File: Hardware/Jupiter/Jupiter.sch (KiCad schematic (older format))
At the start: 0 parts

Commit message: Start schematic diagram by placing the first IC components.
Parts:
- added MD?: Board_RPi_CM3lite_200pConnector, _, symbol Board_RPi_CM3lite_200pConnector
- added U?: STM32F070CBT6, symbol STM32F070CBT6
- added U?: ENC28J60, symbol ENC28J60
- added U?: CY7C65632, symbol CY7C65632
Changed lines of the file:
@@
 LIBS:contrib
 LIBS:valves
+LIBS:stm32f070cbt6
+LIBS:MIC2026
+LIBS:KiCADinfo_RPi-modules
+LIBS:enc28j60
+LIBS:cy7c65632
+LIBS:503182-1852
+LIBS:Jupiter-cache
 EELAYER 25 0
 EELAYER END
-$Descr USLetter 11000 8500
+$Descr A2 23386 16535
 encoding utf-8
 Sheet 1 1
@@
 Comment4 ""
 $EndDescr
+$Comp
+L Board_RPi_CM3lite_200pConnector MD?
+U 1 1 5B60D14B
+P 3550 8200
+F 0 "MD?" H 4275 575 50  0000 C CNN
+F 1 "Board_RPi_CM3lite_200pConnector" H 3550 15825 50  0000 C CNN
+F 2 "_" H 3550 8200 10  0001 C CNN
+F 3 "_" H 3550 8200 10  0001 C CNN
+F 4 "_" H 3550 8200 10  0001 C CNN "Manf#"
+F 5 "_" H 3550 8200 10  0001 C CNN "Manf"
+F 6 "_" H 3550 8200 10  0001 C CNN "Optn"
+	1    3550 8200
+	1    0    0    -1
+$EndComp
+$Comp
+L STM32F070CBT6 U?
+U 1 1 5B60D344
+P 9350 3400
+F 0 "U?" H 9350 2650 60  0000 C CNN
+F 1 "STM32F070CBT6" H 9350 2950 60  0000 C CNN
+F 2 "" H 9350 3400 60  0001 C CNN
+F 3 "" H 9350 3400 60  0001 C CNN
+	1    9350 3400
+	1    0    0    -1
+$EndComp
+$Comp
+L ENC28J60 U?
+U 1 1 5B60D397
+P 9100 7900
+F 0 "U?" H 9100 6100 60  0000 C CNN
+F 1 "ENC28J60" H 9100 8400 60  0000 C CNN
+F 2 "" H 9100 7500 60  0000 C CNN
+F 3 "" H 9100 7500 60  0000 C CNN
+	1    9100 7900
+	1    0    0    -1
+$EndComp
+$Comp
+L CY7C65632 U?
+U 1 1 5B60D432
+P 14500 3900
+F 0 "U?" H 14500 3750 60  0000 C CNN
+F 1 "CY7C65632" H 14500 3900 60  0000 C CNN
+F 2 "" H 14500 3900 60  0000 C CNN
+F 3 "" H 14500 3900 60  0000 C CNN
+	1    14500 3900
+	1    0    0    -1
+$EndComp
 $EndSCHEMATC

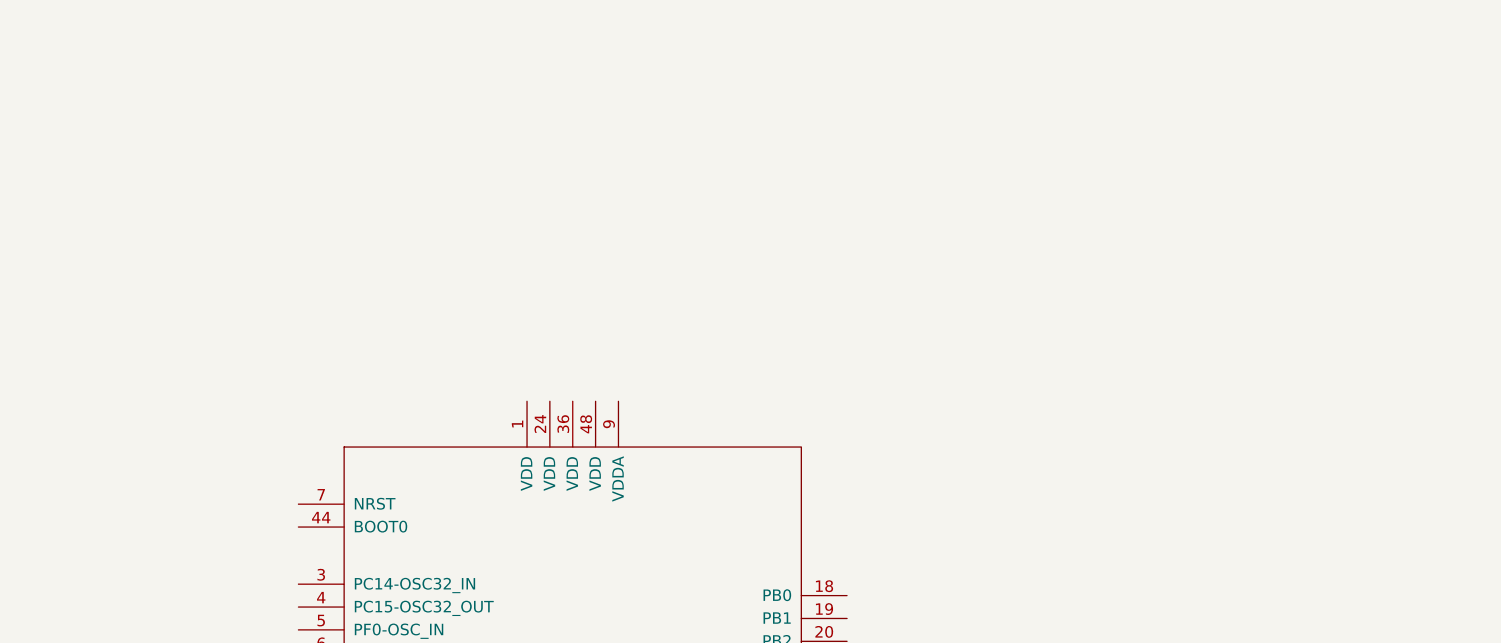
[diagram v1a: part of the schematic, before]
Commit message: Add a power regulator for providing both 3.3v and 1.8v to board.
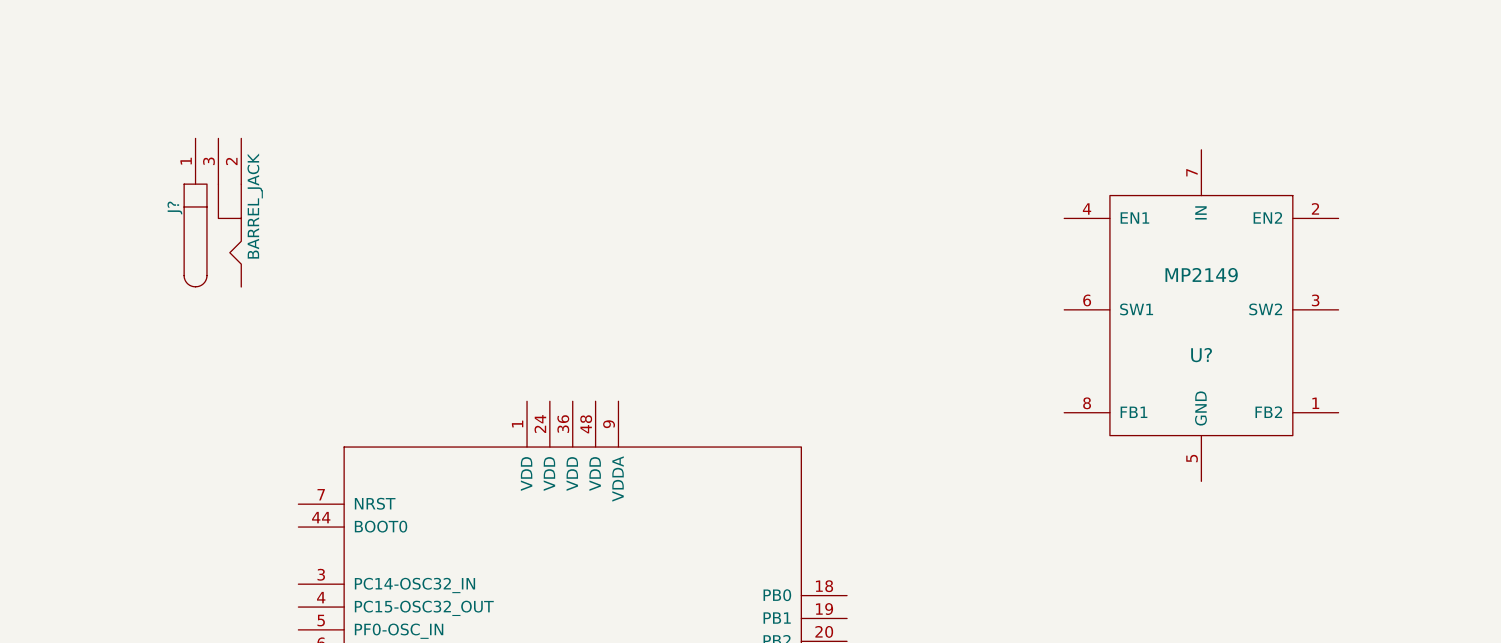
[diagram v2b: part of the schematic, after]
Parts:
- added J?: BARREL_JACK, symbol BARREL_JACK
- added U?: MP2149, symbol MP2149
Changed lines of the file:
@@
 LIBS:cy7c65632
 LIBS:503182-1852
+LIBS:MP2149
 LIBS:Jupiter-cache
 EELAYER 25 0
@@
 	1    0    0    -1
 $EndComp
+$Comp
+L BARREL_JACK J?
+U 1 1 5B60D3BC
+P 7800 1350
+F 0 "J?" H 7800 1545 50  0000 C CNN
+F 1 "BARREL_JACK" H 7800 1195 50  0000 C CNN
+F 2 "" H 7800 1350 50  0001 C CNN
+F 3 "" H 7800 1350 50  0001 C CNN
+	1    7800 1350
+	0    -1   -1   0
+$EndComp
+$Comp
+L MP2149 U?
+U 1 1 5B60D5AD
+P 12100 1800
+F 0 "U?" H 12100 1600 60  0000 C CNN
+F 1 "MP2149" H 12100 1950 60  0000 C CNN
+F 2 "" H 12100 1800 60  0000 C CNN
+F 3 "" H 12100 1800 60  0000 C CNN
+	1    12100 1800
+	1    0    0    -1
+$EndComp

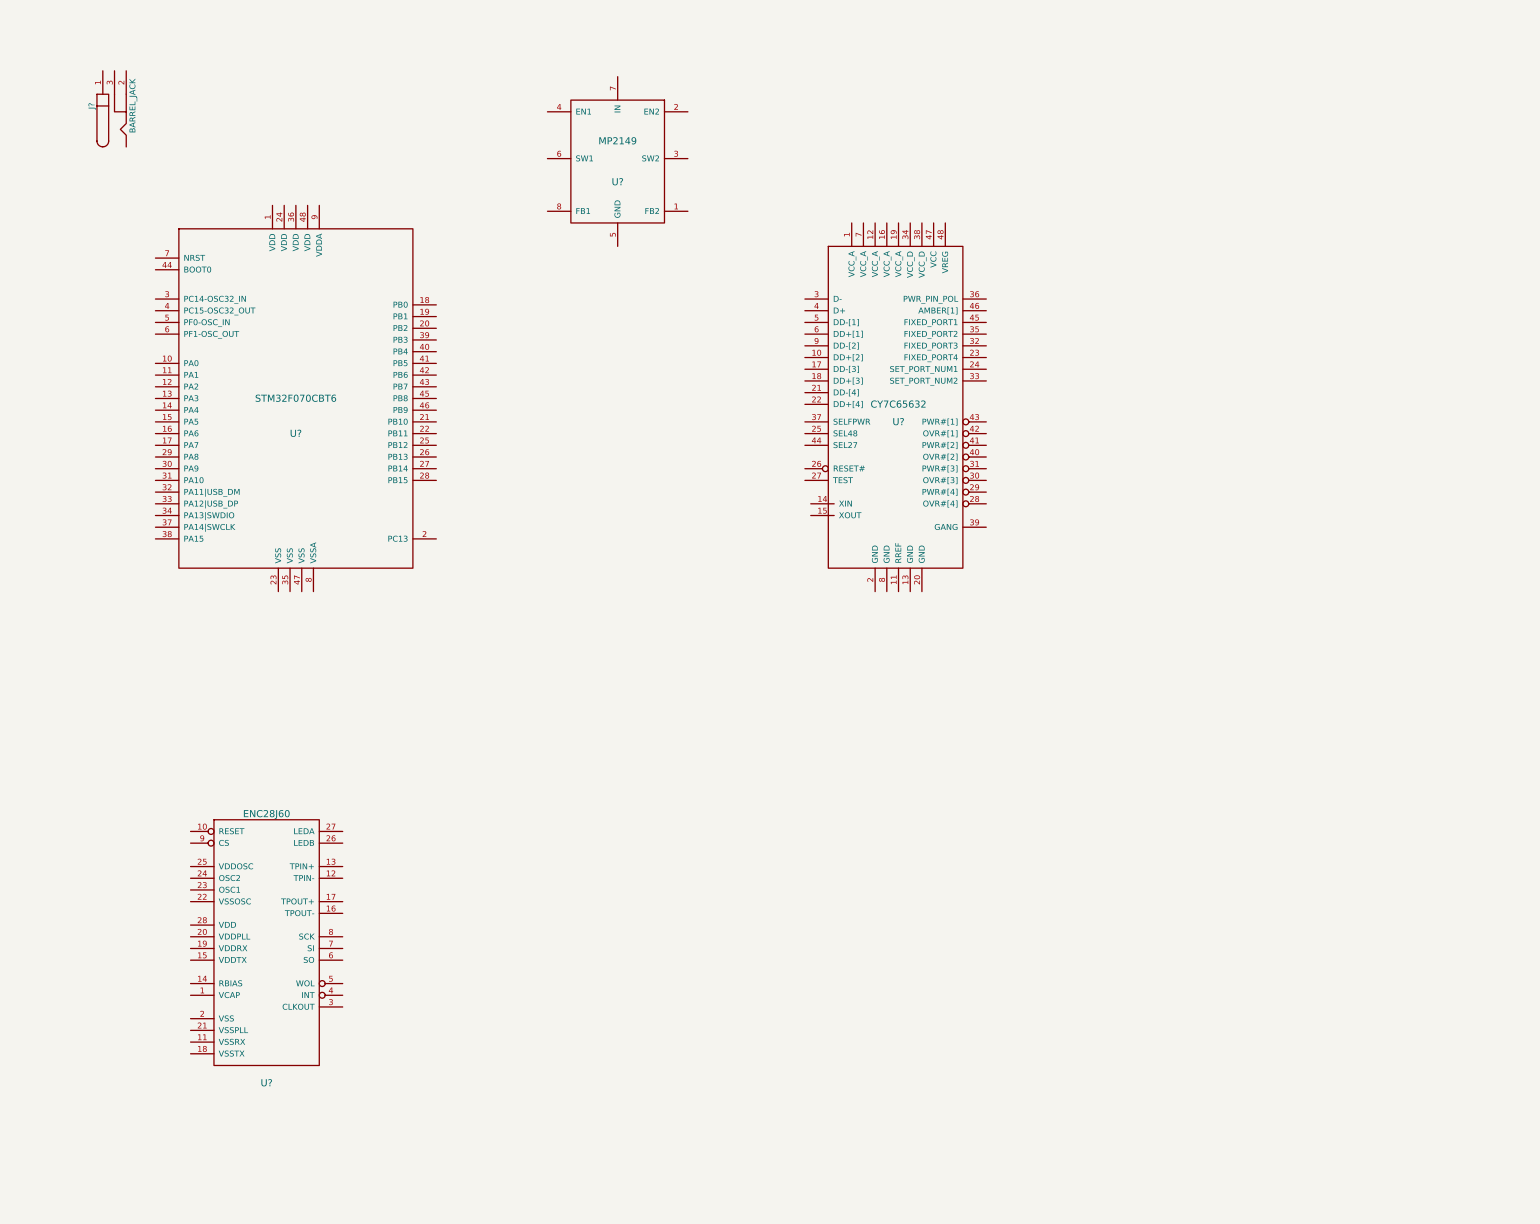
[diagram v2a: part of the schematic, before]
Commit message: Add power input and start work on network adapter chip.
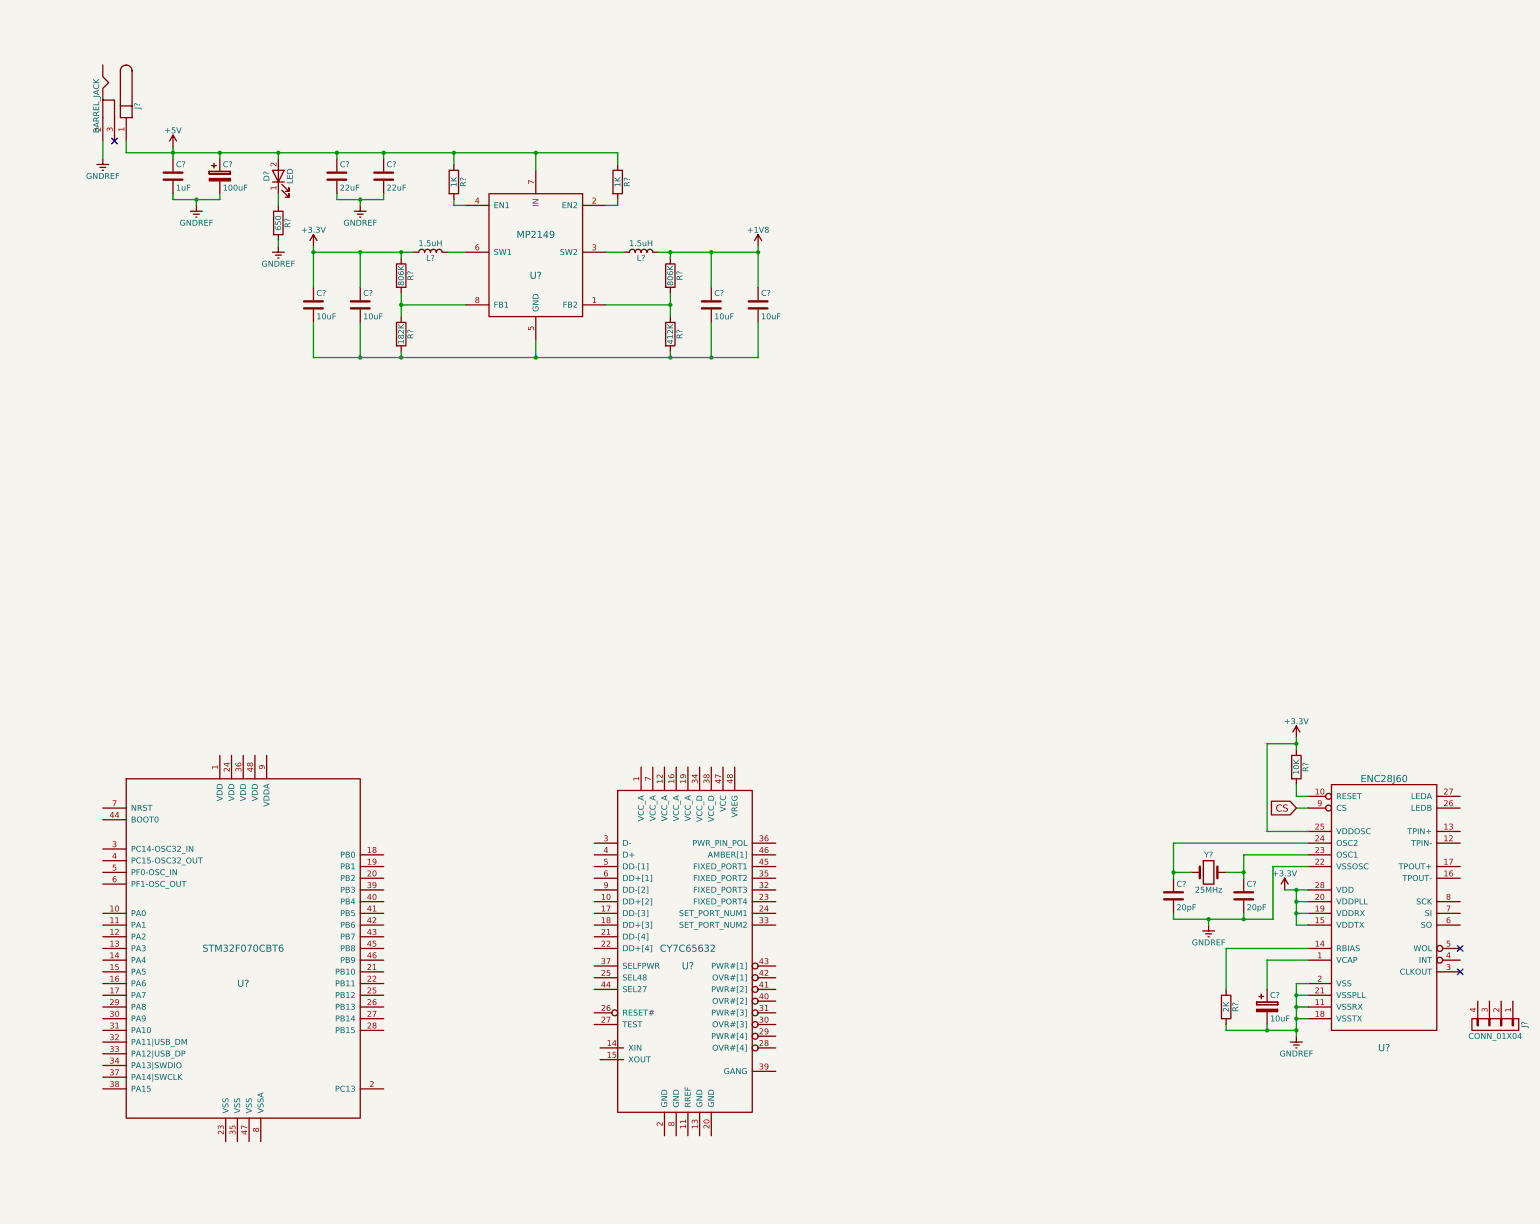
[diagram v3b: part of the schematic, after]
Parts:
- added C?: 1uF, symbol C
- added C?: 100uF, symbol CP
- added C? (x2): 22uF, symbol C
- added C? (x4): 10uF, symbol C
- added C?: 10uF, symbol CP
- added C? (x2): 20pF, symbol C
- added D?: LED, symbol LED
- added J?: CONN_01X04, symbol CONN_01X04
- added L? (x2): 1.5uH, symbol L
- added R?: 650, symbol R
- added R? (x2): 806K, symbol R
- added R?: 182K, symbol R
- added R?: 412K, symbol R
- added R? (x2): 1K, symbol R
- added R?: 10K, symbol R
- added R?: 2K, symbol R
- added Y?: 25MHz, symbol Crystal
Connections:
- net at U?.1 (VCAP): now also C?.1
- net at U?.10 (RESET): now also R?.2
- net GNDREF: now reaches U?.11 (VSSRX)
- net GNDREF: now also J?.2, U?.18 (VSSTX), U?.2 (VSS), U?.21 (VSSPLL), U?.22 (VSSOSC), C?.2, C?.2, C?.2, C?.2, C?.2, C?.2, C?.2, R?.2, R?.2
- net at U?.14 (RBIAS): now also R?.1
- net +3V3: now reaches U?.15 (VDDTX)
- net +3V3: now also U?.19 (VDDRX), U?.20 (VDDPLL), U?.25 (VDDOSC), U?.28 (VDD), C?.1, C?.1, L?.1, R?.1, R?.1
- net at U?.23 (OSC1): now also C?.1, Y?.2
- net at U?.24 (OSC2): now also C?.1, Y?.1
- net CS: now reaches U?.9 (CS)
- net +5V: now reaches J?.1
- net +5V: now also U?.7 (IN), C?.1, C?.1, C?.1, C?.1, D?.2 (A), R?.1, R?.1
- net at U?.1 (FB2): now also R?.1, R?.2
- net at U?.2 (EN2): now also R?.2
- net at U?.3 (SW2): now also L?.1
- net at U?.4 (EN1): now also R?.2
- net at U?.5 (GND): now also C?.2, C?.2, C?.2, C?.2, R?.2, R?.2
- net at U?.6 (SW1): now also L?.2
- net at U?.8 (FB1): now also R?.1, R?.2
- new net: D?.1 (K), R?.1
- new net +1V8: C?.1, C?.1, L?.2, R?.1
- no-connect marks 0 -> 3
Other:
- moved on the sheet: J?, U?

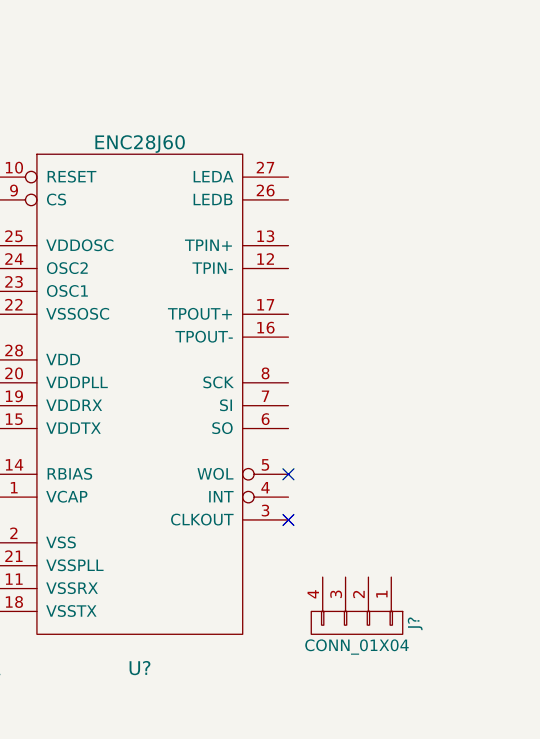
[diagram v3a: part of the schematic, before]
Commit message: Finish detail on network interface chip.
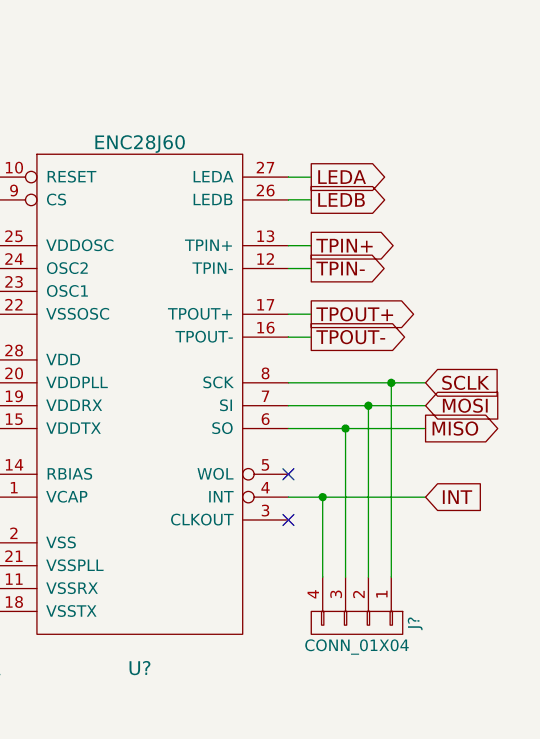
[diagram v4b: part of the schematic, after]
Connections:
- net TPIN-: now reaches U?.12 (TPIN-)
- net TPIN+: now reaches U?.13 (TPIN+)
- net TPOUT-: now reaches U?.16 (TPOUT-)
- net TPOUT+: now reaches U?.17 (TPOUT+)
- net LEDB: now reaches U?.26 (LEDB)
- net LEDA: now reaches U?.27 (LEDA)
- net INT: now reaches U?.4 (INT)
- net INT: now also J?.4 (P4)
- net MISO: now reaches U?.6 (SO)
- net MISO: now also J?.3 (P3)
- net MOSI: now reaches U?.7 (SI)
- net MOSI: now also J?.2 (P2)
- net SCLK: now reaches U?.8 (SCK)
- net SCLK: now also J?.1 (P1)
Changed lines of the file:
@@
 	17650 7550 18000 7550
 Connection ~ 17900 6800
+Text GLabel 19400 7250 2    60   Output ~ 0
+LEDA
+Text GLabel 19400 7350 2    60   Output ~ 0
+LEDB
+Text GLabel 19400 7550 2    60   Output ~ 0
+TPIN+
+Text GLabel 19400 7650 2    60   Output ~ 0
+TPIN-
+Text GLabel 19400 7850 2    60   Output ~ 0
+TPOUT+
+Text GLabel 19400 7950 2    60   Output ~ 0
+TPOUT-
+Wire Wire Line
+	19400 7250 19300 7250
+Wire Wire Line
+	19400 7350 19300 7350
+Wire Wire Line
+	19400 7550 19300 7550
+Wire Wire Line
+	19400 7650 19300 7650
+Wire Wire Line
+	19400 7850 19300 7850
+Wire Wire Line
+	19400 7950 19300 7950
+Text GLabel 19900 8350 2    60   Output ~ 0
+MISO
+Text GLabel 19900 8250 2    60   Input ~ 0
+MOSI
+Text GLabel 19900 8150 2    60   Input ~ 0
+SCLK
+Text GLabel 19900 8650 2    60   Input ~ 0
+INT
+Wire Wire Line
+	19900 8650 19300 8650
+Wire Wire Line
+	19900 8350 19300 8350
+Wire Wire Line
+	19900 8250 19300 8250
+Wire Wire Line
+	19900 8150 19300 8150
+Wire Wire Line
+	19450 9000 19450 8650
+Connection ~ 19450 8650
+Wire Wire Line
+	19550 9000 19550 8350
+Connection ~ 19550 8350
+Wire Wire Line
+	19650 9000 19650 8250
+Connection ~ 19650 8250
+Wire Wire Line
+	19750 9000 19750 8150
+Connection ~ 19750 8150
 $EndSCHEMATC

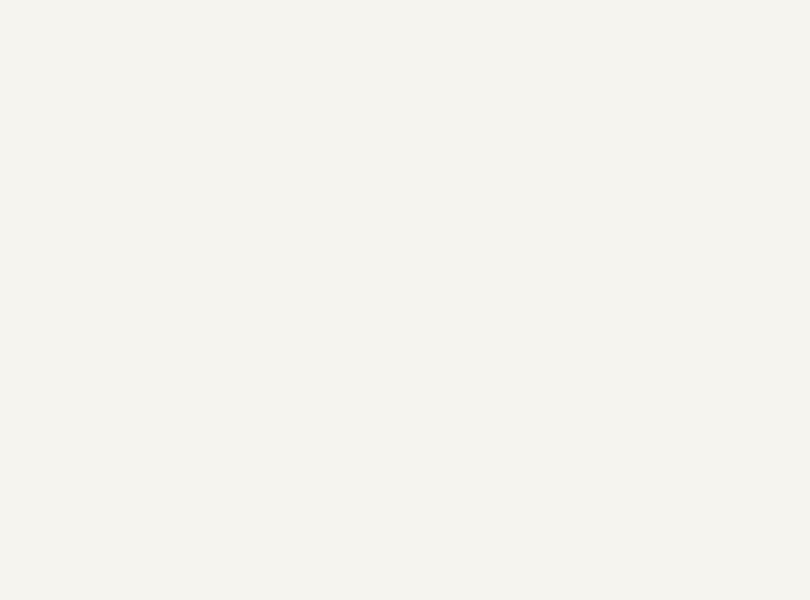
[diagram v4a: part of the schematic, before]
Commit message: Add an Ethernet connector jack.
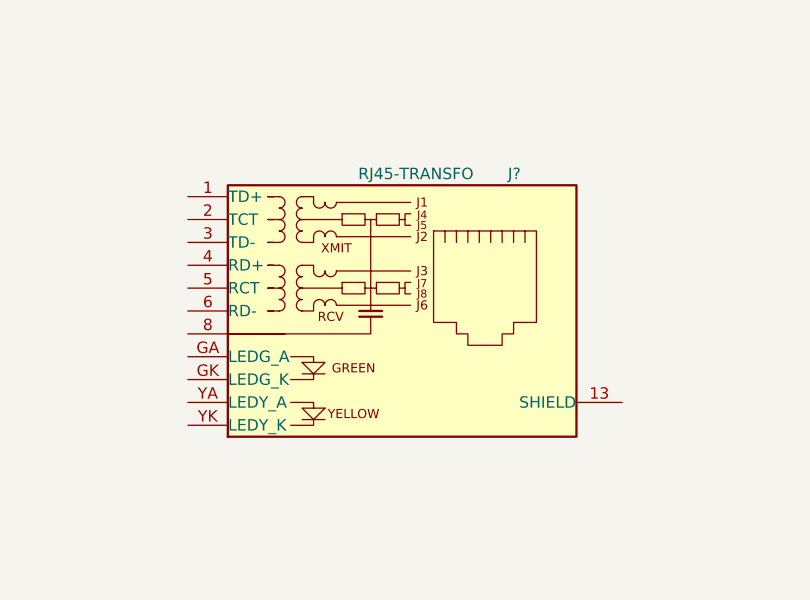
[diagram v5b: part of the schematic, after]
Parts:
- added J?: RJ45-TRANSFO, symbol RJ45-TRANSFO
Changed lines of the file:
@@
 	19750 9000 19750 8150
 Connection ~ 19750 8150
+$Comp
+L RJ45-TRANSFO J?
+U 1 1 5B62B049
+P 18800 4250
+F 0 "J?" H 18900 4850 50  0000 L CNN
+F 1 "RJ45-TRANSFO" H 18750 4850 50  0000 R CNN
+F 2 "" H 18800 4250 50  0001 C CNN
+F 3 "" H 18800 4250 50  0001 C CNN
+	1    18800 4250
+	1    0    0    -1
+$EndComp
 $EndSCHEMATC
